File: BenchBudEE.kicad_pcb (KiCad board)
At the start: 4 copper layers, 165.1 x 63.5 mm, 36 parts, among them K1 1461069-5, P1 24 Pin MiniFit Jr, P2 CONN_2, P3 CONN_3X2, P4 12 Pin Terminal Block, P5 3-Pin TB, Q1 2N3904, U1 LTV-816S, U2 MCP3901, U3 LMT84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

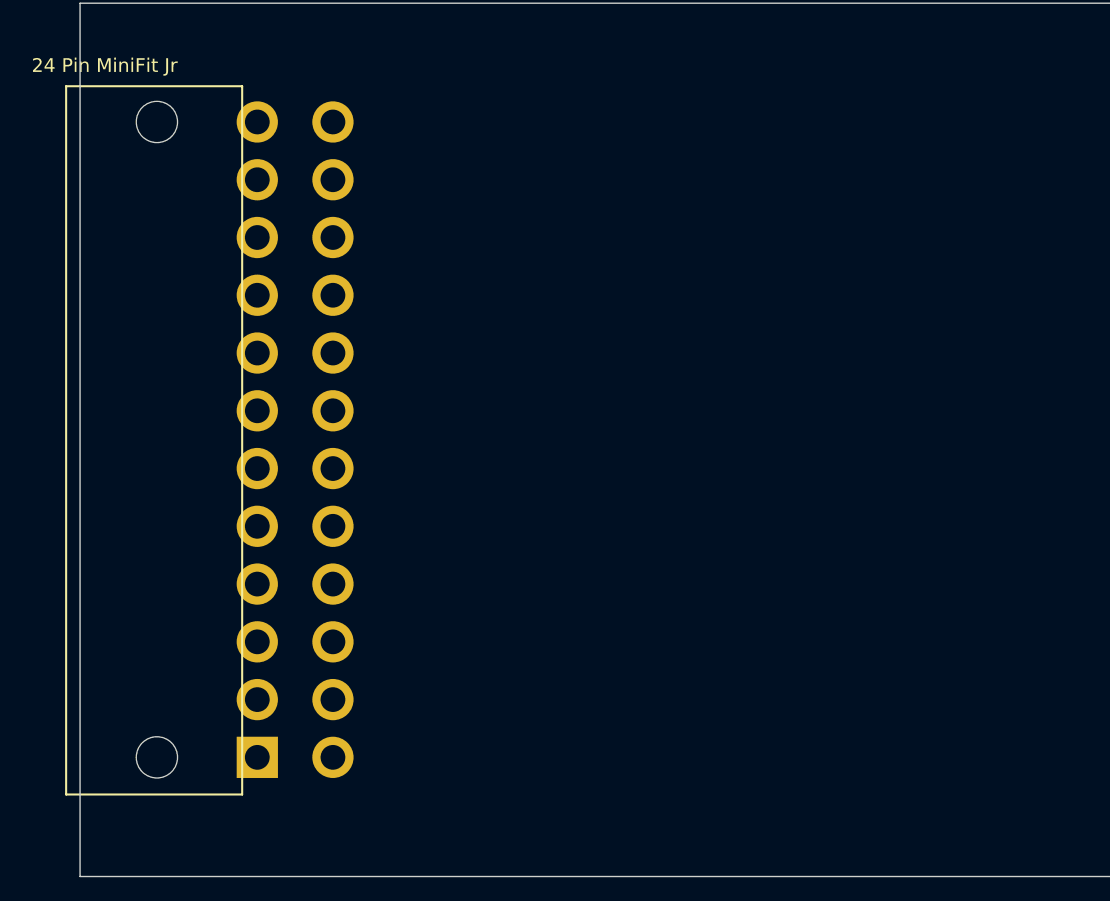
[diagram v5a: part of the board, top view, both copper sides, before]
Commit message: Placed arduino module
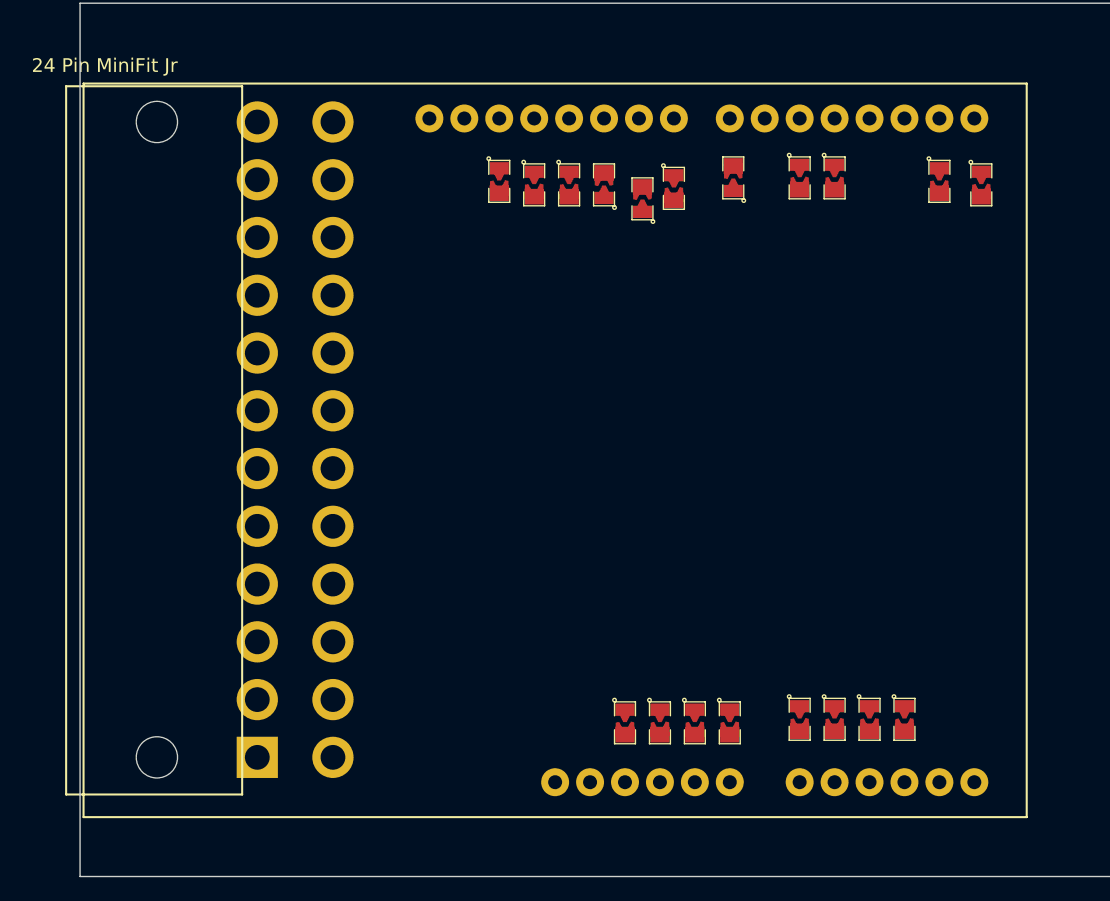
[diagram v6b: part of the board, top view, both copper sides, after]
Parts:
- added ARD1: ARDUINO_PINS, BenchBudEE:arduino, F.Cu at (192.0, 170.9)
- added R28: R, BenchBudEE:SM0805_BLOB_BRIDGE, F.Cu at (174.2, 166.6)
- added R29: R, BenchBudEE:SM0805_BLOB_BRIDGE, F.Cu at (179.3, 166.4)
- added R30: R, BenchBudEE:SM0805_BLOB_BRIDGE, F.Cu at (181.9, 166.4)
- added R31: R, BenchBudEE:SM0805_BLOB_BRIDGE, F.Cu at (184.4, 166.4)
- added R32: R, BenchBudEE:SM0805_BLOB_BRIDGE, F.Cu at (186.9, 166.4)
- added R33: R, BenchBudEE:SM0805_BLOB_BRIDGE, F.Cu at (189.5, 127.3)
- added R34: R, BenchBudEE:SM0805_BLOB_BRIDGE, F.Cu at (157.5, 127.3)
- added R35: R, BenchBudEE:SM0805_BLOB_BRIDGE, F.Cu at (160.0, 127.5)
- added R36: R, BenchBudEE:SM0805_BLOB_BRIDGE, F.Cu at (162.6, 127.5)
- added R37: R, BenchBudEE:SM0805_BLOB_BRIDGE, F.Cu at (165.1, 127.5)
- added R38: R, BenchBudEE:SM0805_BLOB_BRIDGE, F.Cu at (167.9, 128.5)
- added R39: R, BenchBudEE:SM0805_BLOB_BRIDGE, F.Cu at (170.2, 127.8)
- added R40: R, BenchBudEE:SM0805_BLOB_BRIDGE, F.Cu at (174.5, 127.0)
- added R41: R, BenchBudEE:SM0805_BLOB_BRIDGE, F.Cu at (192.5, 127.5)
- added R45: R, BenchBudEE:SM0805_BLOB_BRIDGE, F.Cu at (179.3, 127.0)
- added R46: R, BenchBudEE:SM0805_BLOB_BRIDGE, F.Cu at (181.9, 127.0)
- added R49: R, BenchBudEE:SM0805_BLOB_BRIDGE, F.Cu at (166.6, 166.6)
- added R50: R, BenchBudEE:SM0805_BLOB_BRIDGE, F.Cu at (169.2, 166.6)
- added R51: R, BenchBudEE:SM0805_BLOB_BRIDGE, F.Cu at (171.7, 166.6)

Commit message: more changes?
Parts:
- added C11: C, SMD_Packages:SM0805, B.Cu at (217.2, 175.8)
- added C12: C, SMD_Packages:SM0805, F.Cu at (238.0, 169.4)
- added D5: B130-13-F, Diodes_SMD:Diode-SMA_Handsoldering, F.Cu at (254.3, 172.2)
- added Q2: DMN65D8L-7, SMD_Packages:SOT23GDS, F.Cu at (226.1, 172.0)
- added Q3: AOD476, SMD_Packages:DPAKGDS, F.Cu at (249.9, 165.1)
- added Q4: AOD476, SMD_Packages:DPAKGDS, F.Cu at (259.1, 164.8)
- added R16: R, SMD_Packages:SM0805, B.Cu at (210.3, 171.2)
- added R17: R, SMD_Packages:SM1206, F.Cu at (234.2, 173.2)
- added R52: R, BenchBudEE:SM0805_BLOB_BRIDGE, F.Cu at (185.2, 127.5)
- added R53: R, BenchBudEE:SM0805_BLOB_BRIDGE, F.Cu at (187.5, 129.8)
- added TH5: MINISMDC050F-2, SMD_Packages:SM1812, F.Cu at (243.1, 173.0)
- added U6: MCP4801, SMD_Packages:SO8N, F.Cu at (216.9, 171.7)
- moved C8 19.3 mm to (228.6, 164.6)
- moved R10 19.3 mm to (223.3, 159.8)
- moved R9 19.3 mm to (233.4, 159.8)
- moved R11 19.3 mm to (235.5, 152.1)
- moved C5 19.3 mm to (214.1, 161.0)
- moved C6 19.3 mm to (218.4, 161.0)
- moved C7 19.3 mm to (233.7, 154.7)
- moved C9 19.3 mm to (232.4, 164.6)
- moved P2 19.3 mm to (207.3, 155.4)
- moved P3 19.3 mm to (226.8, 145.5)
- moved R12 19.3 mm to (224.3, 150.6)
- moved R13 19.3 mm to (224.3, 154.7)
- moved R43 19.3 mm to (229.4, 150.6)
- moved R44 19.3 mm to (226.8, 150.6)
- moved R47 19.3 mm to (219.7, 154.9)
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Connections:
- net /Arduino/ADC_CS_N renamed /Arduino/~ADC_CS
- net /Fan/FAN_OUT+ renamed /TerminalBlock/FAN_OUT+
- net /Fan/FAN_OUT- renamed /TerminalBlock/FAN_OUT-
- P4 pad 10: /Fan/TACH_IN -> /TerminalBlock/TACH_IN

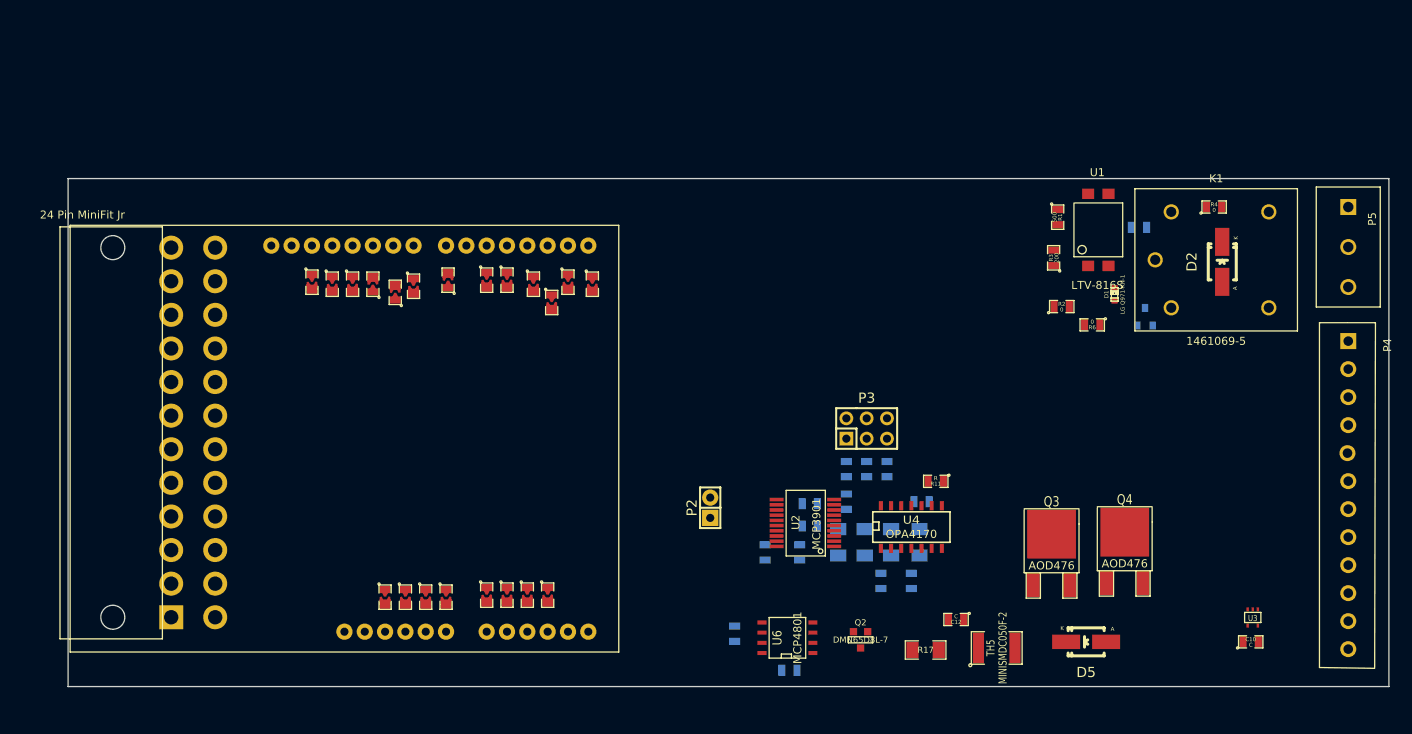
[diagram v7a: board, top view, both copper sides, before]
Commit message: placed power module
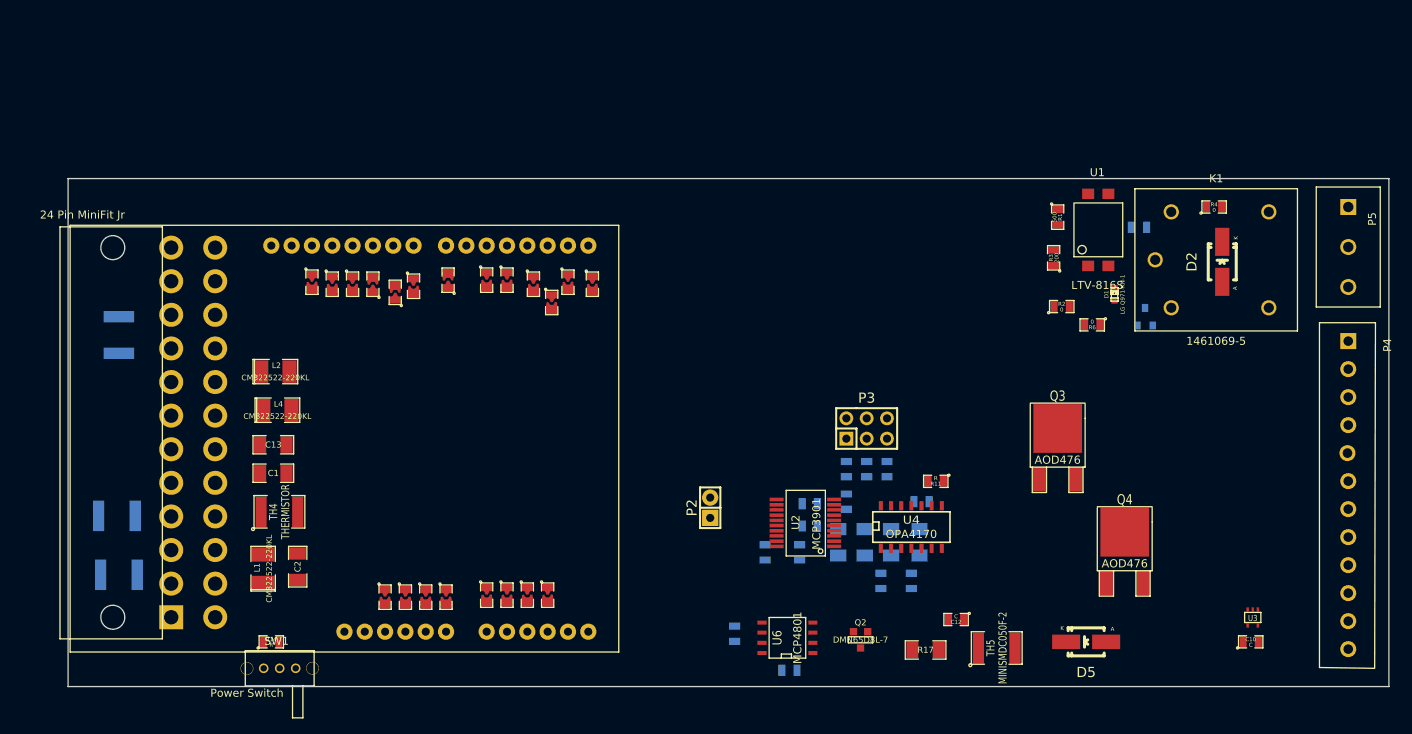
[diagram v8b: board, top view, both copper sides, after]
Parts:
- added C1: C, SMD_Packages:SM1206, F.Cu at (152.7, 151.1)
- added C13: C, SMD_Packages:SM1206, F.Cu at (152.7, 147.6)
- added C2: C, SMD_Packages:SM1206, F.Cu at (155.7, 162.8)
- added L1: CM322522-220KL, SMD_Packages:SM1210L, F.Cu at (151.4, 163.1)
- added L2: CM322522-220KL, SMD_Packages:SM1210L, F.Cu at (152.9, 138.4)
- added L4: CM322522-220KL, SMD_Packages:SM1210L, F.Cu at (153.2, 143.3)
- added R14: R, SMD_Packages:SM0805, F.Cu at (152.4, 172.2)
- added SW1: Power Switch, BenchBudEE:BB_powerSwitch, F.Cu at (149.4, 175.5)
- added TH1: THERMISTOR, SMD_Packages:SM1812, B.Cu at (133.3, 163.8)
- added TH2: THERMISTOR, SMD_Packages:SM1812, B.Cu at (133.1, 156.5)
- added TH3: THERMISTOR, SMD_Packages:SM1812, B.Cu at (133.3, 133.9)
- added TH4: THERMISTOR, SMD_Packages:SM1812, F.Cu at (153.4, 156.0)
- moved Q3 13.2 mm to (250.7, 151.9)
